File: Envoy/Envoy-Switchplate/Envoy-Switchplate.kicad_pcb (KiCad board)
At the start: 2 copper layers, 95.4 x 95.4 mm, 26 parts

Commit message: add PCB identifier
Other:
- board text added: "Envoy by JeJeff - switch plate - rev 0.2"
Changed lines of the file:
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@@
     (effects (font (size 0.85 0.85) (thickness 0.15)) (justify mirror))
+  )
+  (gr_text "Envoy by JeJeff - switch plate - rev 0.2" (at 140.6655 123.45075) (layer "B.Mask")
+    (effects (font (size 1 1) (thickness 0.15)) (justify mirror))
   )
   (zone (net 0) (net_name "") (layer "F.Cu") (hatch edge 0.508)

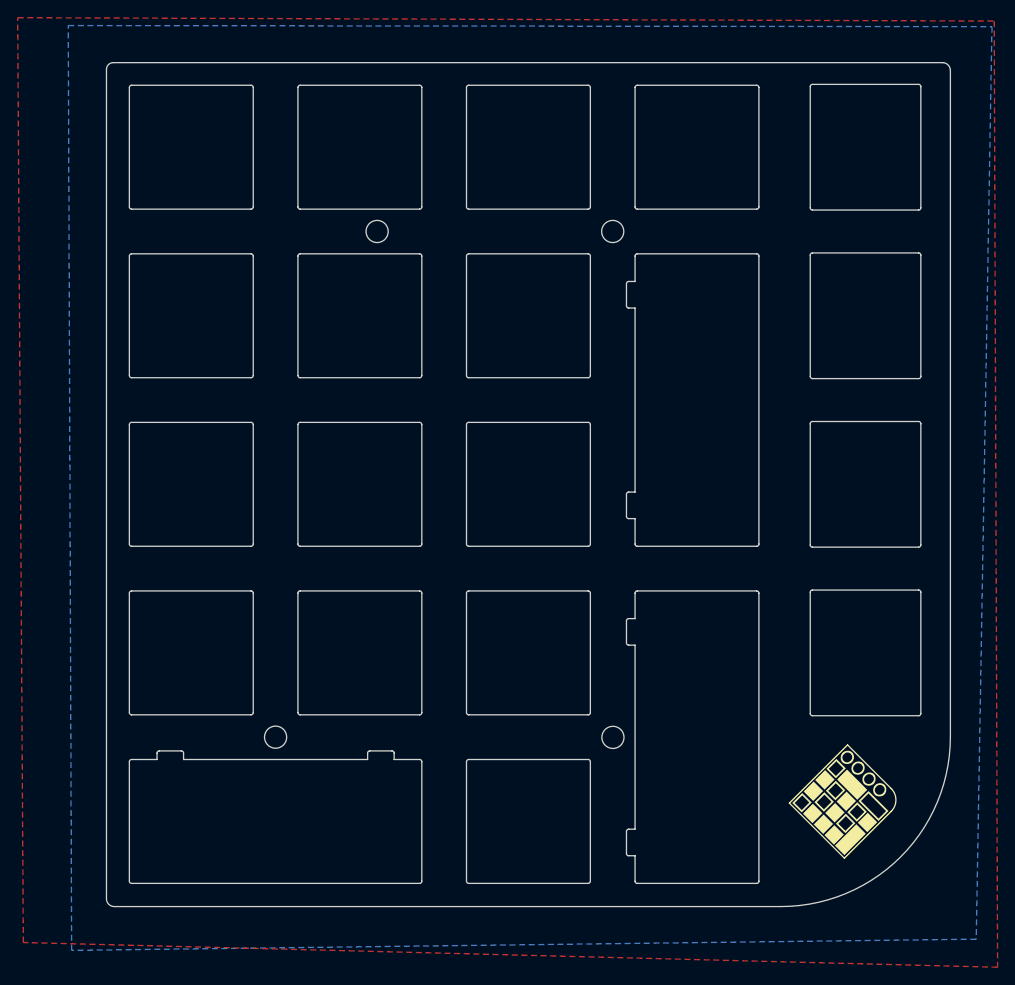
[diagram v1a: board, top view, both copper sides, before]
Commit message: More tweaks to the switchplate cutouts, make switchplate float instead of the PCB, move diodes to give more space to stabs
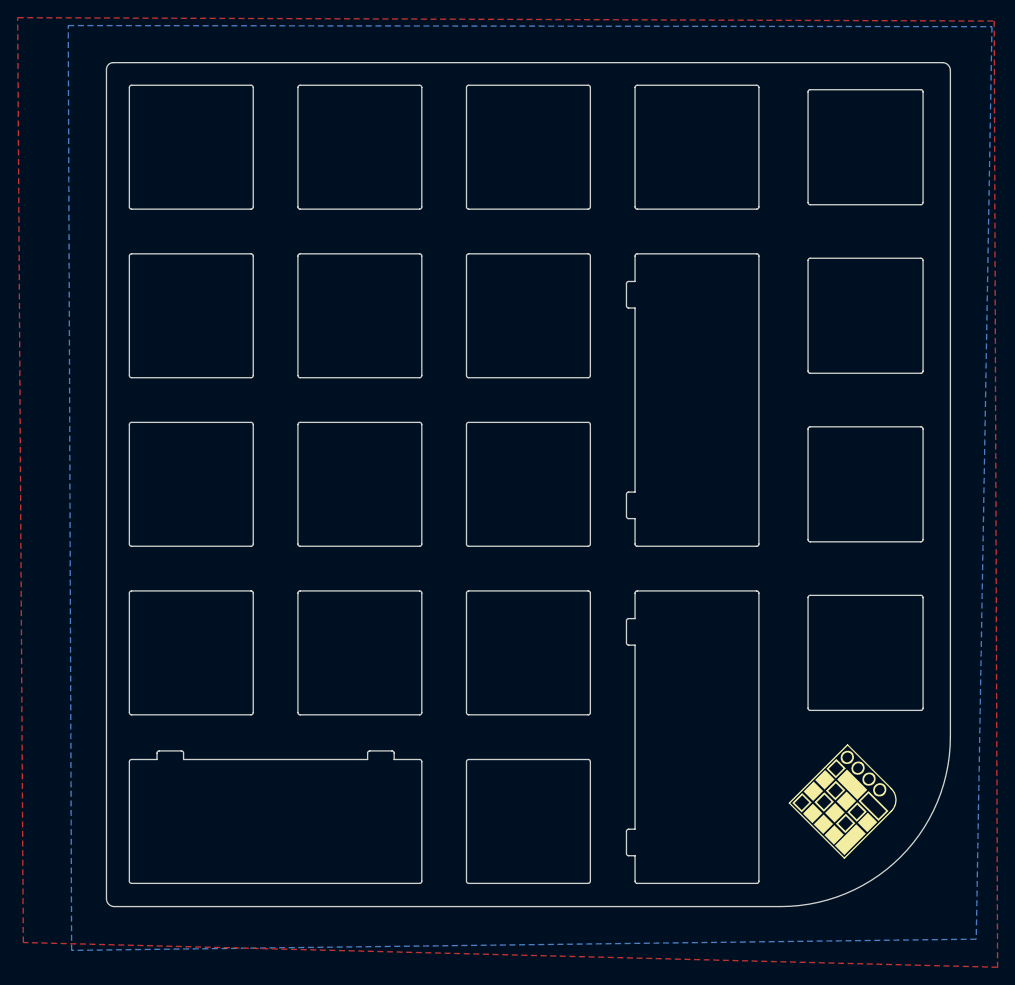
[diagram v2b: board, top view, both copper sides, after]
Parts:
- removed H1, H2, H3, H4: MountingHole, MountingHole:MountingHole_2.5mm
- ENC1, ENC2, ENC3, ENC4: footprint Envoy:RotaryEncoder_Cutout -> Envoy:RotaryEncoder_Cutout_12.5x12.5_fillets
- MX1, MX10, MX11, MX13, MX14, MX15, MX19, MX2, MX3, MX4, MX5, MX6, MX7, MX9: footprint Envoy:MX_Switch_Cutout_Square -> Envoy:MX_Switch_Cutout_Square_fillets
